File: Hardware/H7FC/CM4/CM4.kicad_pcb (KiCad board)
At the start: 4 copper layers, 57 x 79.3 mm, 127 parts, among them IC1 ADP7156ARDZ-3.3-R7, IC2 STM32H747IIT6, J1 UART, J10 Conn_01x04, J11 Conn_01x06, J12 TSW-101-08-G-T-RA, J13 USB_B_Micro, J14 SWDIO, J15 Micro_SD_Card, J16 Conn_01x03_Female, J2 USB_C_Receptacle_USB2.0, J3 Conn_01x02, J4 32K101-400L5, J5 TSW-101-08-G-T-RA, J6 TSW-101-08-G-T-RA, J7 TSW-101-08-G-T-RA, J8 TSW-101-08-G-T-RA, J9 Conn_01x02, Q1 AO3401A, Q2 BC817W, U1 BMP280, U2 MAX-M8Q, U3 LSM9DS1, U4 USBLC6-2SC6, Y1 16MHz

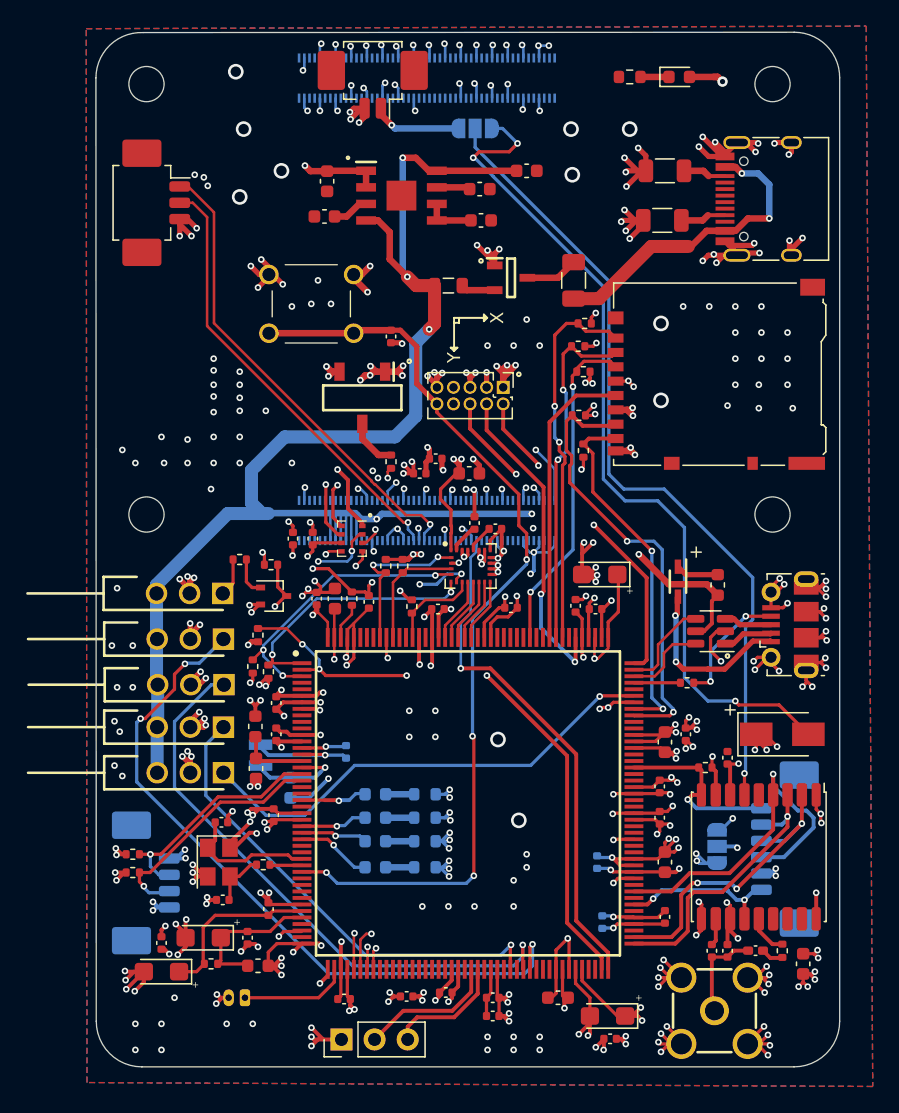
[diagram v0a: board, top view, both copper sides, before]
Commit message: Set initial cUbeMX Cconfig. Fixed Clock and GPIO bug
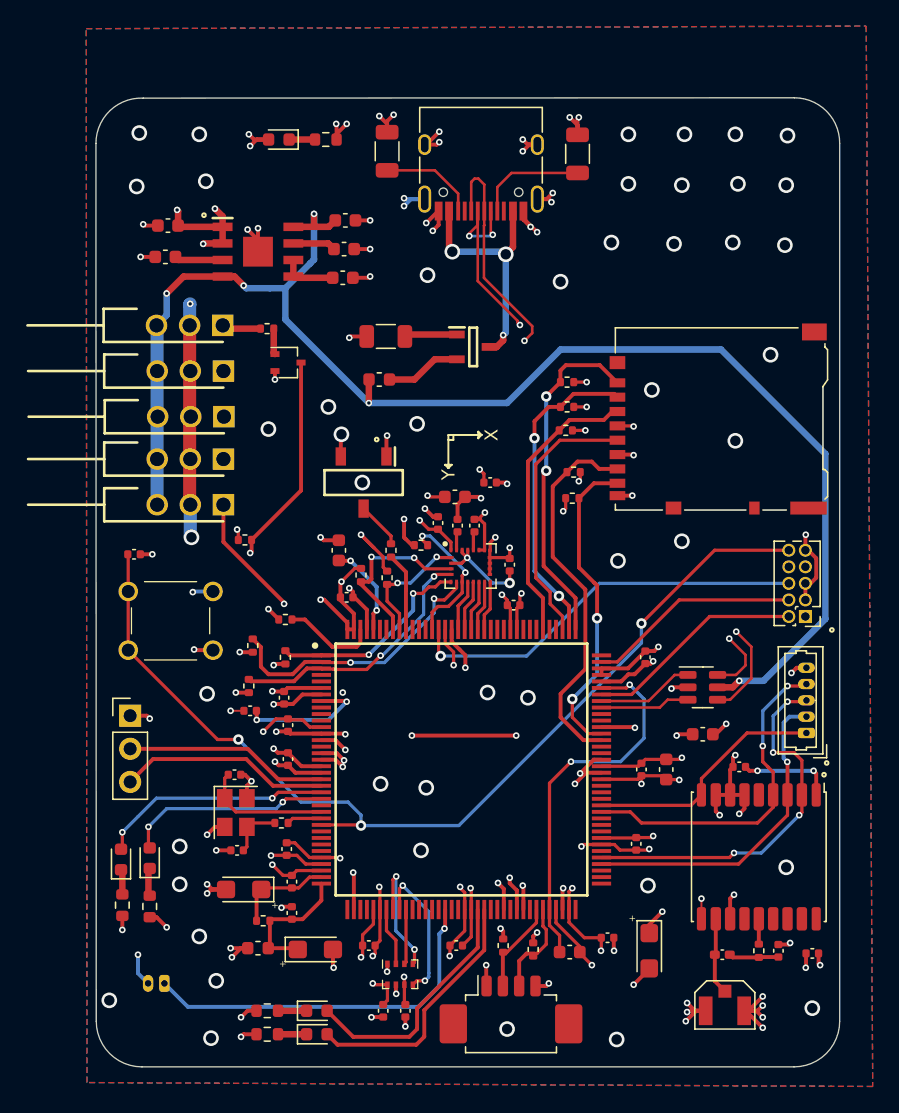
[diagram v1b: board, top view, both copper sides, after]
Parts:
- removed C18, C20, C21, C22, C23, C24, C48: 100n, Capacitor_SMD:C_0402_1005Metric
- removed C41, C43: 10u, Capacitor_SMD:C_0603_1608Metric
- removed C42: 220p, Capacitor_SMD:C_0402_1005Metric
- removed C44: 1u_X5R_0603, Capacitor_SMD:C_0603_1608Metric
- removed C47: 4.7u, Capacitor_Tantalum_SMD:CP_EIA-3216-18_Kemet-A
- removed C49: 2.2u, Capacitor_SMD:C_0603_1608Metric
- removed D2: SS14, Diode_SMD:D_SMA
- removed D3: SD103AWS-TP, SamacSys_Parts:SOD2512X115N
- removed F1: Polyfuse, Fuse:Fuse_1206_3216Metric
- removed FB3: 100 @100Mhz, Inductor_SMD:L_0603_1608Metric
- removed FB4: 18 @100Mhz, Inductor_SMD:L_0603_1608Metric
- removed J11: Conn_01x06, Connector_Molex:Molex_PicoBlade_53261-0671_1x06-1MP_P1.25mm_Horizontal
- removed J13: USB_B_Micro, Connector_USB:USB_Micro-B_Molex-105017-0001
- removed J4: 32K101-400L5, SamacSys_Parts:32K101-400L5
- removed JP1: Jumper_3_Open, Jumper:SolderJumper-3_P1.3mm_Open_RoundedPad1.0x1.5mm
- removed JP2: SolderJumper_3_Open, Jumper:SolderJumper-3_P1.3mm_Open_RoundedPad1.0x1.5mm
- removed L3: 2.2uH, SamacSys_Parts:LQM2MPN1R0NG0L
- removed Module1: ComputeModule4-CM4, CM4IO:Raspberry-Pi-4-Compute-Module
- removed R14: 10k, Resistor_SMD:R_0402_1005Metric
- removed R21: 560, Resistor_SMD:R_0402_1005Metric
- added R2: 470, Resistor_SMD:R_1206_3216Metric, F.Cu at (145.2, 66.3)
- C16: value 100n -> 1u
- C17: value 100n -> 1u_X5R_0603; footprint Capacitor_SMD:C_0402_1005Metric -> Capacitor_SMD:C_0603_1608Metric
- C33, D4, D5, D6, D7, J10, R22, R23, R24, R25: moved to F.Cu
- C4: value 1u -> 10u
- C45, C46: value 4.7u -> 2.2u
- C9: value 22p -> 100n
- FB1: value 600 @ 100MHz -> 100 @ 100MHz; footprint Inductor_SMD:L_0805_2012Metric -> Inductor_SMD:L_0603_1608Metric
- IC2: value STM32H747IIT6 -> STM32H745ZIT6; footprint SamacSys_Parts:QFP50P2600X2600X160-176N -> SamacSys_Parts:QFP50P2200X2200X160-144N
- J1: value UART -> Conn_Coaxial; footprint Connector_Molex:Molex_PicoBlade_53261-0371_1x03-1MP_P1.25mm_Horizontal -> CM4IO:BWIPX-1-001E
- J3: value Conn_01x02 -> Conn_01x05; footprint Connector_Molex:Molex_PicoBlade_53261-0271_1x02-1MP_P1.25mm_Horizontal -> Connector_Molex:Molex_PicoBlade_53047-0510_1x05_P1.25mm_Vertical
- moved J1 76.1 mm to (171.2, 118.0), turned to 90 degrees
- moved J3 60.3 mm to (177.4, 96.7), turned to 90 degrees
- moved C6 36.9 mm to (146.7, 118.0), turned to -90 degrees
- moved C5 36.9 mm to (145.0, 118.0), turned to -90 degrees
- moved R6 34.1 mm to (137.5, 88.0), turned to 0 degrees
- moved U1 33.6 mm to (146.3, 115.2), turned to 0 degrees
- moved R17 31.6 mm to (156.5, 113.3), turned to -90 degrees
- moved D1 31.1 mm to (137.0, 51.2), turned to 180 degrees
- moved J10 30.4 mm to (154.8, 118.5), turned to 0 degrees
- moved J16 29.6 mm to (125.6, 95.4), turned to 0 degrees
- moved J14 29.1 mm to (177.4, 87.8), turned to 180 degrees
- moved R18 28.9 mm to (154.2, 113.0), turned to 90 degrees
- moved C16 27.6 mm to (134.8, 95.0), turned to 180 degrees
- moved S1 26.6 mm to (128.7, 88.1)
- moved C52 25.8 mm to (125.9, 83.0), turned to 180 degrees
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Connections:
- net /5V renamed +5V
- C1 pad 1: /+3.3V -> VDDLDO
- C10 pad 1: /+3.3V -> VDDLDO
- C11 pad 1: /+3.3V -> VDDLDO
- C15 pad 1: /+3.3V -> VDDLDO
- C16 pad 1: /+3.3V -> /MCU/VBAT
- C17 pad 1: /+3.3V -> VDDLDO
- C19 pad 1: /+3.3V -> VDDLDO
- C29 pad 1: /+3.3V -> VDDLDO
- C30 pad 1: /+3.3V -> VDDLDO
- C31 pad 1: /+3.3V -> VDDLDO
- C32 pad 1: /+3.3V -> VDDLDO
- C33 pad 1: /+3.3V -> VDDLDO
- C34 pad 1: /+3.3V -> VDDLDO
- C35 pad 1: /+3.3V -> VDDLDO
- C36 pad 1: /+3.3V -> VDDLDO
- C37 pad 1: /+3.3V -> VDDLDO
- C38 pad 1: /+3.3V -> VDDLDO
- C39 pad 1: /+3.3V -> VDDLDO
- C4 pad 1: /+3.3V -> VDDLDO
- C40 pad 1: /+3.3V -> VDDLDO
- C45 pad 1: /MCU/VCAP1 -> VCAP
- C46 pad 1: /MCU/VCAP1 -> VCAP
- C5 pad 1: /+3.3V -> VDDLDO
- C6 pad 1: /+3.3V -> VDDLDO
- C7 pad 1: /+3.3V -> VDDLDO
- C8 pad 1: /+3.3V -> VDDLDO
- C9 pad 1: Net-(C12-Pad1) -> VDDLDO
- C9 pad 2: Net-(C9-Pad2) -> GND
- D1 pad 2: /+3.3V -> VDDLDO
- FB2 pad 1: /+3.3V -> VDDLDO
- IC1 pad 1: /+3.3V -> VDDLDO
- IC1 pad 2: /+3.3V -> VDDLDO
- IC2 pad 10: no_connect_96 -> unconnected-(IC2-Pad10)
- IC2 pad 100: GND -> /MCU/USB_D_N
- IC2 pad 101: /+3.3V -> /MCU/USB_D_P
- IC2 pad 102: /+3.3V -> /MCU/SWDIO
- IC2 pad 103: no_connect_97 -> VCAP
- IC2 pad 104: no_connect_98 -> GND
- IC2 pad 105: GND -> VDDLDO
- IC2 pad 106: no_connect_99 -> VDDLDO
- IC2 pad 107: no_connect_100 -> /MCU/SWCLK
- IC2 pad 108: /+3.3V -> unconnected-(IC2-Pad108)
- IC2 pad 109: GND -> /MCU/SDMMC_D2
- IC2 pad 11: no_connect_101 -> unconnected-(IC2-Pad11)
- IC2 pad 110: no_connect_102 -> /MCU/SDMMC_D3
- IC2 pad 111: no_connect_103 -> /MCU/SDMMC_CK
- IC2 pad 112: GND -> unconnected-(IC2-Pad112)
- IC2 pad 113: /+3.3V -> unconnected-(IC2-Pad113)
- IC2 pad 114: no_connect_104 -> /MCU/SDMMC_CMD
- IC2 pad 115: no_connect_105 -> unconnected-(IC2-Pad115)
- IC2 pad 116: M8Q_NRST -> unconnected-(IC2-Pad116)
- IC2 pad 117: no_connect_106 -> unconnected-(IC2-Pad117)
- IC2 pad 118: no_connect_107 -> GND
- IC2 pad 119: GND -> VDDLDO
- IC2 pad 120: /+3.3V -> unconnected-(IC2-Pad120)
- IC2 pad 121: /+3.3V -> unconnected-(IC2-Pad121)
- IC2 pad 122: no_connect_108 -> unconnected-(IC2-Pad122)
- IC2 pad 123: no_connect_109 -> LSM9DS1_DEN_AG
- IC2 pad 124: /MCU/SDMMC_D0 -> LSM9DS1_INT2_AG
- IC2 pad 125: /MCU/SDMMC_D1 -> LSM9DS1_INT1_AG
- IC2 pad 126: /+3.3V -> LSM9DS1_INT_M
- IC2 pad 127: TIM1_CH1 -> LSM9DS1_DRDY_M
- IC2 pad 128: no_connect_110 -> GND
- IC2 pad 129: /MCU/USB_OTG_ID -> VDDLDO
- IC2 pad 13: /+3.3V -> VDDLDO
- IC2 pad 130: /MCU/USB_D_N -> /MCU/SWO
- IC2 pad 131: /MCU/USB_D_P -> LSM9DS1_CS_M
- IC2 pad 132: /MCU/SWDIO -> unconnected-(IC2-Pad132)
- IC2 pad 133: /MCU/VCAP1 -> unconnected-(IC2-Pad133)
- IC2 pad 134: GND -> unconnected-(IC2-Pad134)
- IC2 pad 135: /MCU/VCAP1 -> /MCU/BOOT0
- IC2 pad 136: /+3.3V -> I2C1_SCL
- IC2 pad 137: GND -> I2C1_SDA
- IC2 pad 138: /MCU/SWCLK -> unconnected-(IC2-Pad138)
- IC2 pad 139: no_connect_111 -> unconnected-(IC2-Pad139)
- IC2 pad 140: /MCU/SDMMC_D2 -> VCAP
- IC2 pad 141: /MCU/SDMMC_D3 -> GND
- IC2 pad 142: /MCU/SDMMC_CK -> Net-(IC2-Pad142)
- IC2 pad 143: no_connect_112 -> VDDLDO
- IC2 pad 144: no_connect_113 -> VDDLDO
- IC2 pad 15: /MCU/VLXSMPS -> unconnected-(IC2-Pad15)
- IC2 pad 16: /MCU/VDDSMPS -> GND
- IC2 pad 17: /MCU/VCAP1 -> GND
- IC2 pad 18: I2C2_SDA -> GND
- IC2 pad 19: I2C2_SCL -> VDDLDO
- IC2 pad 20: no_connect_126 -> UART7_RX
- IC2 pad 21: no_connect_127 -> UART7_TX
- IC2 pad 22: /MCU/LED_A -> /MCU/LED_C
- IC2 pad 23: no_connect_128 -> /MCU/LED_D
- IC2 pad 24: GND -> unconnected-(IC2-Pad24)
- IC2 pad 25: /+3.3V -> /MCU/HSE_IN
- IC2 pad 26: /MCU/LED_B -> /MCU/HSE_OUT
- IC2 pad 27: /MCU/LED_C -> /MCU/NRST
- IC2 pad 28: /MCU/LED_D -> unconnected-(IC2-Pad28)
- IC2 pad 29: no_connect_129 -> unconnected-(IC2-Pad29)
- IC2 pad 30: no_connect_130 -> unconnected-(IC2-Pad30)
- IC2 pad 31: /MCU/HSE_IN -> unconnected-(IC2-Pad31)
- IC2 pad 32: /MCU/HSE_OUT -> VDDLDO
- IC2 pad 33: /MCU/NRST -> GND
- IC2 pad 34: no_connect_131 -> GND
- IC2 pad 35: no_connect_132 -> /MCU/VREF+
- IC2 pad 36: no_connect_133 -> /MCU/+3.3VA
- IC2 pad 37: no_connect_134 -> unconnected-(IC2-Pad37)
- IC2 pad 38: GND -> SBUS_RX
- IC2 pad 39: /MCU/VREF+ -> unconnected-(IC2-Pad39)
- IC2 pad 4: no_connect_135 -> unconnected-(IC2-Pad4)
- IC2 pad 40: /MCU/+3.3VA -> unconnected-(IC2-Pad40)
- IC2 pad 41: no_connect_136 -> GND
- IC2 pad 42: SBUS_RX -> VDDLDO
- IC2 pad 43: no_connect_137 -> SPI1_NCS
- IC2 pad 44: /+3.3V -> SPI1_SCK
- IC2 pad 45: GND -> SPI1_MISO
- IC2 pad 46: ANALOG_IN -> SPI1_MOSI
- IC2 pad 47: GND -> unconnected-(IC2-Pad47)
- IC2 pad 48: /+3.3V -> unconnected-(IC2-Pad48)
- IC2 pad 49: SPI1_NCS -> unconnected-(IC2-Pad49)
- IC2 pad 5: no_connect_138 -> unconnected-(IC2-Pad5)
- IC2 pad 50: SPI1_SCK -> unconnected-(IC2-Pad50)
- IC2 pad 51: SPI1_MISO -> unconnected-(IC2-Pad51)
- IC2 pad 52: SPI1_MOSI -> ANALOG_IN
- IC2 pad 53: no_connect_139 -> unconnected-(IC2-Pad53)
- IC2 pad 54: no_connect_140 -> unconnected-(IC2-Pad54)
- IC2 pad 55: no_connect_141 -> GND
- IC2 pad 56: no_connect_142 -> VDDLDO
- IC2 pad 57: no_connect_143 -> /MCU/LED_A
- IC2 pad 58: no_connect_144 -> /MCU/LED_B
- IC2 pad 59: no_connect_145 -> unconnected-(IC2-Pad59)
- IC2 pad 60: no_connect_146 -> unconnected-(IC2-Pad60)
- IC2 pad 61: no_connect_147 -> TIM1_CH2
- IC2 pad 62: no_connect_148 -> unconnected-(IC2-Pad62)
- IC2 pad 63: no_connect_149 -> TIM1_CH3
- IC2 pad 64: GND -> TIM1_CH4
- IC2 pad 65: /+3.3V -> unconnected-(IC2-Pad65)
- IC2 pad 66: no_connect_150 -> I2C2_SCL
- IC2 pad 67: UART7_RX -> I2C2_SDA
- IC2 pad 68: UART7_TX -> VCAP
- IC2 pad 69: no_connect_151 -> GND
- IC2 pad 7: /+3.3V -> VDDLDO
- IC2 pad 70: GND -> VDDLDO
- IC2 pad 71: /+3.3V -> VDDLDO
- IC2 pad 72: no_connect_152 -> unconnected-(IC2-Pad72)
- IC2 pad 73: TIM1_CH2 -> unconnected-(IC2-Pad73)
- IC2 pad 74: no_connect_153 -> unconnected-(IC2-Pad74)
- IC2 pad 75: TIM1_CH3 -> unconnected-(IC2-Pad75)
- IC2 pad 76: TIM1_CH4 -> M8Q_RX
- IC2 pad 77: no_connect_154 -> M8Q_TX
- IC2 pad 78: no_connect_155 -> unconnected-(IC2-Pad78)
- IC2 pad 79: no_connect_156 -> VDDLDO
- IC2 pad 8: /+3.3V -> /MCU/VBAT
- IC2 pad 80: /MCU/VCAP1 -> GND
- IC2 pad 81: GND -> unconnected-(IC2-Pad81)
- IC2 pad 82: /MCU/VCAP1 -> unconnected-(IC2-Pad82)
- IC2 pad 83: GND -> unconnected-(IC2-Pad83)
- IC2 pad 84: /+3.3V -> M8Q_PPS
- IC2 pad 85: no_connect_157 -> M8Q_NRST
- IC2 pad 86: no_connect_158 -> unconnected-(IC2-Pad86)
- IC2 pad 87: PI_GPIO13_RX_5 -> unconnected-(IC2-Pad87)
- IC2 pad 88: PI_GPIO12_TX_5 -> unconnected-(IC2-Pad88)
- IC2 pad 89: M8Q_RX -> GND
- IC2 pad 9: no_connect_159 -> unconnected-(IC2-Pad9)
- IC2 pad 90: M8Q_TX -> VDDLDO
- IC2 pad 91: no_connect_160 -> VDDLDO
- IC2 pad 92: /+3.3V -> VDDLDO
- IC2 pad 93: GND -> unconnected-(IC2-Pad93)
- IC2 pad 94: no_connect_161 -> unconnected-(IC2-Pad94)
- IC2 pad 95: M8Q_GPS_LNA_EN -> /MCU/SDMMC_D0
- IC2 pad 96: no_connect_162 -> /MCU/SDMMC_D1
- IC2 pad 97: M8Q_PPS -> TIM1_CH1
- IC2 pad 98: no_connect_163 -> unconnected-(IC2-Pad98)
- IC2 pad 99: /+3.3V -> unconnected-(IC2-Pad99)
- J1 pad 1: /CM4 GPIO/GPIO_15_RX -> Net-(J1-Pad1)
- J1 pad 2: /CM4 GPIO/GPIO_14_TX -> GND
- J10 pad 1: /+3.3V -> VDDLDO
- J14 pad 1: /+3.3V -> VDDLDO
- J14 pad 7: no_connect_164 -> unconnected-(J14-Pad7)
- J14 pad 8: no_connect_165 -> unconnected-(J14-Pad8)
- J15 pad 4: /+3.3V -> VDDLDO
- J2 pad A6: no_connect_166 -> /Power/USB_D+
- J2 pad A7: no_connect_167 -> /Power/USB_D-
- J2 pad A8: no_connect_168 -> unconnected-(J2-PadA8)
- J2 pad B6: no_connect_169 -> /Power/USB_D+
- J2 pad B7: no_connect_170 -> /Power/USB_D-
- J2 pad B8: no_connect_171 -> unconnected-(J2-PadB8)
- J3 pad 1: Net-(J3-Pad1) -> M8Q_NRST
- J3 pad 2: GND -> M8Q_RX
- L2 pad 1: Net-(L2-Pad1) -> Net-(C12-Pad1)
- L2 pad 2: Net-(C12-Pad1) -> Net-(J1-Pad1)
- Q1 pad 1: GND -> Net-(Q1-Pad1)
- Q1 pad 3: Net-(F1-Pad2) -> VCC
- R10 pad 1: /+3.3V -> VDDLDO
- R11 pad 2: /+3.3V -> VDDLDO
- R15 pad 1: /+3.3V -> VDDLDO
- R16 pad 2: /+3.3V -> VDDLDO
- R17 pad 1: /+3.3V -> VDDLDO
- R18 pad 2: /+3.3V -> VDDLDO
- R27 pad 2: /+3.3V -> VDDLDO
- R28 pad 2: /+3.3V -> VDDLDO
- R29 pad 2: /+3.3V -> VDDLDO
- R30 pad 2: /+3.3V -> VDDLDO
- R31 pad 2: /+3.3V -> VDDLDO
- R5 pad 2: Net-(L2-Pad1) -> Net-(C12-Pad1)
- R6 pad 1: /+3.3V -> VDDLDO
- R6 pad 2: M8Q_NRST -> Net-(IC2-Pad142)
- R7 pad 1: /+3.3V -> VDDLDO
- R8 pad 1: /+3.3V -> VDDLDO
- R9 pad 1: /+3.3V -> VDDLDO
- S1 pad 2: /MCU/NRST -> GND
- S1 pad 4: GND -> /MCU/NRST
- S2 pad 1: /+3.3V -> VDDLDO
- U1 pad 6: /+3.3V -> VDDLDO
- U1 pad 8: /+3.3V -> VDDLDO
- U2 pad 11: Net-(C9-Pad2) -> Net-(J1-Pad1)
- U2 pad 13: M8Q_GPS_LNA_EN -> unconnected-(U2-Pad13)
- U2 pad 15: (no net) -> unconnected-(U2-Pad15)
- U2 pad 16: no_connect_311 -> unconnected-(U2-Pad16)
- U2 pad 17: no_connect_312 -> unconnected-(U2-Pad17)
- U2 pad 18: Net-(JP2-Pad2) -> unconnected-(U2-Pad18)
- U2 pad 5: no_connect_313 -> unconnected-(U2-Pad5)
- U2 pad 6: M8Q_BATT -> VDDLDO
- U2 pad 7: /+3.3V -> VDDLDO
- U2 pad 8: /+3.3V -> VDDLDO
- U3 pad 1: /+3.3V -> VDDLDO
- U3 pad 22: /+3.3V -> VDDLDO
- U3 pad 23: /+3.3V -> VDDLDO
- U3 pad 3: /+3.3V -> VDDLDO
- U4 pad 1: /MCU/USB_CONN_D- -> /MCU/USB_D_P
- U4 pad 3: /MCU/USB_CONN_D+ -> /MCU/USB_D_N
- U4 pad 4: /MCU/USB_D_P -> /Power/USB_D-
- U4 pad 6: /MCU/USB_D_N -> /Power/USB_D+
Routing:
- net /+3.3V: track 178.7 -> 0.00 mm, vias 101 -> 0
- net GND: track 386.6 -> 212.2 mm, vias 356 -> 144
- net VDDLDO: track 0.00 -> 145.0 mm, vias 0 -> 58
- net /MCU/VCAP1: track 77.7 -> 0.00 mm, vias 4 -> 0
- net VCAP: track 0.00 -> 68.7 mm, vias 0 -> 4
- net Net-(D2-Pad2): track 65.7 -> 0.00 mm, vias 3 -> 0
- net /Power/USB_D-: track 0.00 -> 64.3 mm, vias 0 -> 4
- net M8Q_BATT: track 62.0 -> 0.00 mm, vias 1 -> 0
- net /Power/USB_D+: track 0.00 -> 62.0 mm, vias 0 -> 2
- net PI_GPIO13_RX_5: track 42.0 -> 0.00 mm, vias 2 -> 0
- net PI_GPIO12_TX_5: track 39.4 -> 0.00 mm, vias 1 -> 0
- net /CM4 GPIO/GPIO_15_RX: track 35.7 -> 0.00 mm, vias 1 -> 0
- net /CM4 GPIO/GPIO_14_TX: track 34.2 -> 0.00 mm, vias 1 -> 0
- net SPI1_NCS: track 37.4 -> 4.46 mm, vias 3 -> 0
- net SPI1_MOSI: track 36.0 -> 4.21 mm, vias 2 -> 0
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- added copper zone on In2.Cu, net VDDLDO
- removed copper zone on In2.Cu, net /+3.3V
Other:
- board size 57 x 79.3 mm -> 57 x 74.3 mm
- board text added: "5V"
- board text added: "CM4 FCS | Rev1.1"
- board text added: "NRST"
- board text added: "SIG"
- board text removed: "CM4 FCS | Rev1"
- board text removed: "LNA"
- board text removed: "PI UART"
- board text removed: "RST"
- board text removed: "V+"
- board text removed: "Wireless Keepout"
